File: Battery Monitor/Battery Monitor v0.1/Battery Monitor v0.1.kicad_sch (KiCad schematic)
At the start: 60 parts, among them J1 XT60 M (Vertical), J10 2.54mm 3P, J11 2.54mm 3P, J12 2.54mm 3P, J13 JST-SH 3P, J14 JST-SH 3P, J15 JST-SH 3P, J16 JST-SH 3P, J17 JST-SH 3P, J18 JST-SH 3P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

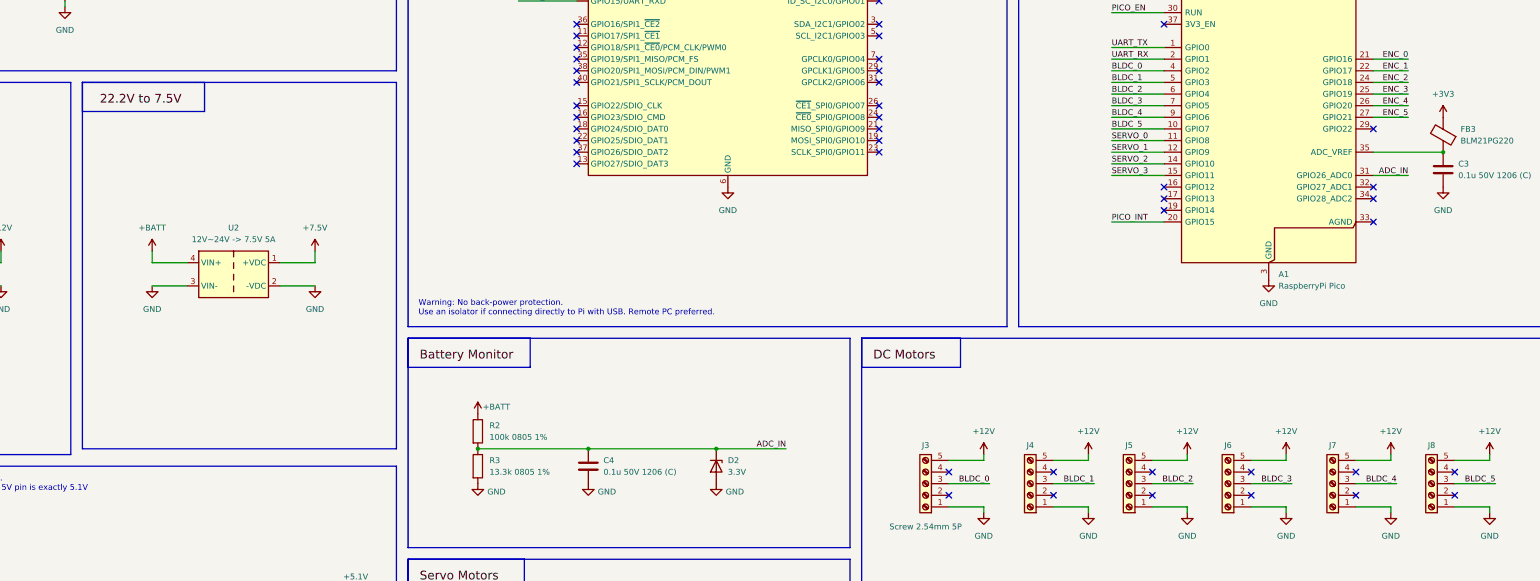
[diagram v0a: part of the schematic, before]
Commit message: Todo: 7.5V buck collides with RPi
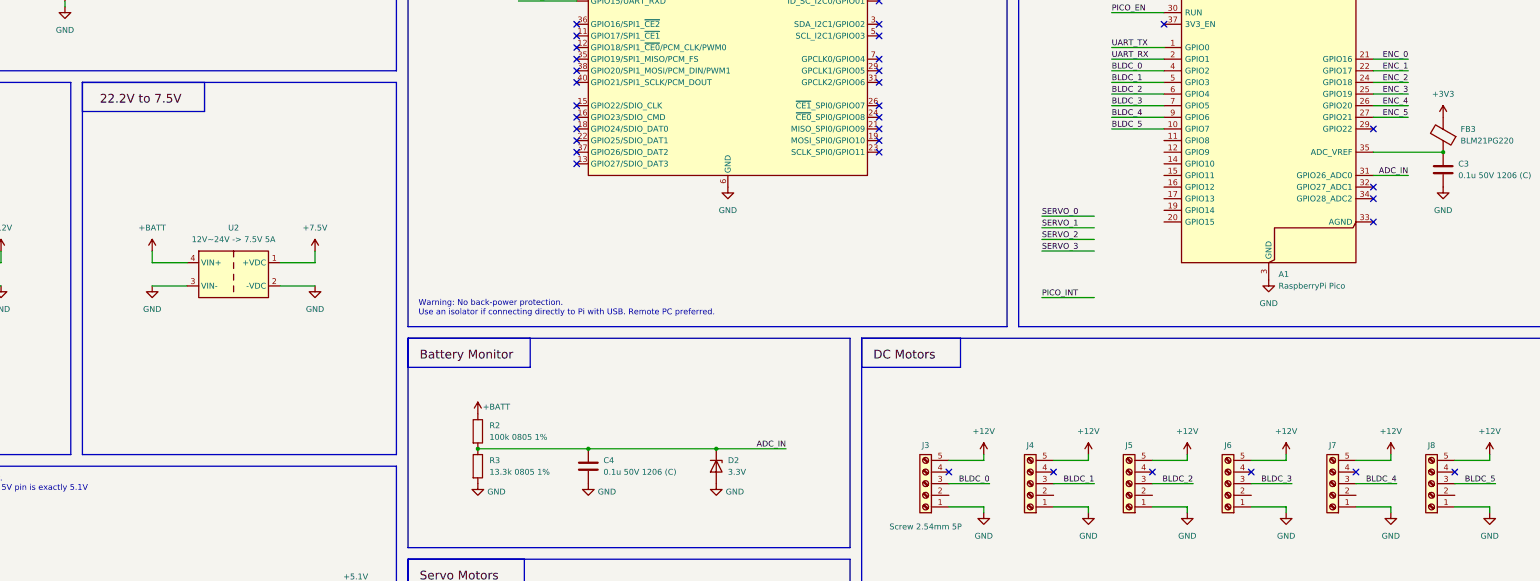
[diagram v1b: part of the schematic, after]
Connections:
- net PICO_INT: no longer A1.20 (GPIO15)
- net SERVO_0: no longer A1.11 (GPIO8)
- net SERVO_1: no longer A1.12 (GPIO9)
- net SERVO_2: no longer A1.14 (GPIO10)
- net SERVO_3: no longer A1.15 (GPIO11)
- no-connect marks 46 -> 37
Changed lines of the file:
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@@
 		(company "HKU ROVER Team")
 		(comment 1 "Designed by: Ilo Japar")
-		(comment 2 "Power")
 	)
 	(rectangle
@@
 	(rectangle
 		(start 83.82 72.39)
-		(end 152.4 152.4)
+		(end 152.4 153.67)
 		(stroke
 			(width 0)
@@
 	)
 	(no_connect
-		(at 320.04 97.79)
-	)
-	(no_connect
 		(at 365.76 102.87)
 	)
@@
 	)
 	(no_connect
-		(at 295.91 162.56)
-	)
-	(no_connect
 		(at 191.77 90.17)
 	)
@@
 	)
 	(no_connect
-		(at 383.54 162.56)
-	)
-	(no_connect
 		(at 257.81 77.47)
 	)
@@
 	)
 	(no_connect
-		(at 361.95 162.56)
-	)
-	(no_connect
 		(at 257.81 52.07)
 	)
@@
 	)
 	(no_connect
-		(at 339.09 162.56)
-	)
-	(no_connect
 		(at 191.77 85.09)
 	)
 	(no_connect
-		(at 320.04 100.33)
-	)
-	(no_connect
 		(at 191.77 64.77)
 	)
@@
 	)
 	(no_connect
-		(at 273.05 162.56)
-	)
-	(no_connect
-		(at 317.5 162.56)
-	)
-	(no_connect
 		(at 257.81 54.61)
 	)
@@
 	)
 	(no_connect
-		(at 320.04 95.25)
-	)
-	(no_connect
 		(at 257.81 69.85)
 	)
@@
 	(wire
 		(pts
+			(xy 293.37 101.6) (xy 304.8 101.6)
+		)
+		(stroke
+			(width 0)
+			(type default)
+		)
+	)
+	(wire
+		(pts
 			(xy 105.41 194.31) (xy 128.27 194.31)
 		)
@@
 	(wire
 		(pts
+			(xy 293.37 119.38) (xy 304.8 119.38)
+		)
+		(stroke
+			(width 0)
+			(type default)
+		)
+	)
+	(wire
+		(pts
 			(xy 320.04 227.33) (xy 323.85 227.33)
 		)
@@
 	(wire
 		(pts
-			(xy 308.61 87.63) (xy 320.04 87.63)
-		)
-		(stroke
-			(width 0)
-			(type default)
-		)
-	)
-	(wire
-		(pts
 			(xy 280.67 166.37) (xy 280.67 165.1)
 		)
@@
 	(wire
 		(pts
-			(xy 308.61 85.09) (xy 320.04 85.09)
-		)
-		(stroke
-			(width 0)
-			(type default)
-		)
-	)
-	(wire
-		(pts
 			(xy 22.86 194.31) (xy 41.91 194.31)
 		)
@@
 	(wire
 		(pts
+			(xy 293.37 106.68) (xy 304.8 106.68)
+		)
+		(stroke
+			(width 0)
+			(type default)
+		)
+	)
+	(wire
+		(pts
 			(xy 218.44 191.77) (xy 218.44 201.93)
 		)
@@
 	(wire
 		(pts
-			(xy 308.61 92.71) (xy 320.04 92.71)
-		)
-		(stroke
-			(width 0)
-			(type default)
-		)
-	)
-	(wire
-		(pts
 			(xy 35.56 186.69) (xy 41.91 186.69)
 		)
@@
 	(wire
 		(pts
+			(xy 293.37 109.22) (xy 304.8 109.22)
+		)
+		(stroke
+			(width 0)
+			(type default)
+		)
+	)
+	(wire
+		(pts
 			(xy 365.76 87.63) (xy 381 87.63)
 		)
@@
 	(wire
 		(pts
+			(xy 293.37 104.14) (xy 304.8 104.14)
+		)
+		(stroke
+			(width 0)
+			(type default)
+		)
+	)
+	(wire
+		(pts
 			(xy 184.15 199.39) (xy 180.34 199.39)
 		)
@@
 		(pts
 			(xy 62.23 246.38) (xy 62.23 243.84)
-		)
-		(stroke
-			(width 0)
-			(type default)
-		)
-	)
-	(wire
-		(pts
-			(xy 308.61 90.17) (xy 320.04 90.17)
-		)
-		(stroke
-			(width 0)
-			(type default)
-		)
-	)
-	(wire
-		(pts
-			(xy 308.61 102.87) (xy 320.04 102.87)
 		)
 		(stroke
@@
 		)
 	)
+	(label "SERVO_0"
+		(at 293.37 101.6 0)
+		(effects
+			(font
+				(size 1.27 1.27)
+			)
+			(justify left bottom)
+		)
+	)
 	(label "PICO_EN"
 		(at 179.07 44.45 0)
@@
 		)
 	)
-	(label "SERVO_1"
-		(at 308.61 87.63 0)
-		(effects
-			(font
-				(size 1.27 1.27)
-			)
-			(justify left bottom)
-		)
-	)
 	(label "BLDC_1"
 		(at 308.61 72.39 0)
@@
 		)
 	)
+	(label "SERVO_1"
+		(at 293.37 104.14 0)
+		(effects
+			(font
+				(size 1.27 1.27)
+			)
+			(justify left bottom)
+		)
+	)
 	(label "DC Motors"
 		(at 256.54 133.35 0)
@@
 		)
 	)
-	(label "SERVO_3"
-		(at 308.61 92.71 0)
-		(effects
-			(font
-				(size 1.27 1.27)
-			)
-			(justify left bottom)
-		)
-	)
 	(label "BLDC_5"
 		(at 308.61 82.55 0)
@@
 		)
 	)
-	(label "PICO_INT"
-		(at 308.61 102.87 0)
-		(effects
-			(font
-				(size 1.27 1.27)
-			)
-			(justify left bottom)
-		)
-	)
 	(label "UART_RX"
 		(at 179.07 54.61 0)
@@
 		)
 	)
+	(label "PICO_INT"
+		(at 293.37 119.38 0)
+		(effects
+			(font
+				(size 1.27 1.27)
+			)
+			(justify left bottom)
+		)
+	)
 	(label "BLDC_4"
 		(at 308.61 80.01 0)
@@
 	)
 	(label "SERVO_2"
-		(at 308.61 90.17 0)
+		(at 293.37 106.68 0)
 		(effects
 			(font
@@
 		)
 	)
-	(label "SERVO_0"
-		(at 308.61 85.09 0)
-		(effects
-			(font
-				(size 1.27 1.27)
-			)
-			(justify left bottom)
-		)
-	)
 	(label "BLDC_1"
 		(at 304.8 160.02 180)
@@
 		(effects
 			(font
+				(size 1.27 1.27)
+			)
+			(justify left bottom)
+		)
+	)
+	(label "SERVO_3"
+		(at 293.37 109.22 0)
+		(effects
+			(font
